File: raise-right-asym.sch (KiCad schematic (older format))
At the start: 83 parts, among them IC1 ATTINY88-A, P1 CONN_01X04, P2 CONN_01X04, P4 CONN_01X04, P6 CONN_02X03, SW1 SW_PUSH, SW10 SW_PUSH, SW11 SW_PUSH, SW12 SW_PUSH, SW13 SW_PUSH, SW14 SW_PUSH, SW15 SW_PUSH, SW16 SW_PUSH, SW17 SW_PUSH, SW18 SW_PUSH, SW19 SW_PUSH, SW2 SW_PUSH, SW20 SW_PUSH, SW21 SW_PUSH, SW22 SW_PUSH, SW23 SW_PUSH, SW24 SW_PUSH, SW25 SW_PUSH, SW26 SW_PUSH, SW27 SW_PUSH, SW28 SW_PUSH, SW29 SW_PUSH, SW3 SW_PUSH, SW30 SW_PUSH, SW31 SW_PUSH, SW32 SW_PUSH, SW33 SW_PUSH, SW34 SW_PUSH, SW4 SW_PUSH, SW5 SW_PUSH, SW6 SW_PUSH, SW7 SW_PUSH, SW8 SW_PUSH, SW9 SW_PUSH

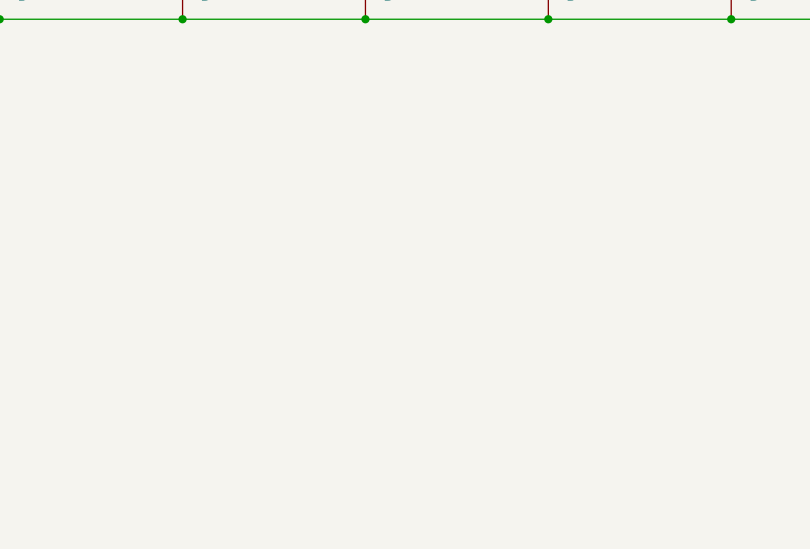
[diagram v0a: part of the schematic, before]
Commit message: note on number of keys
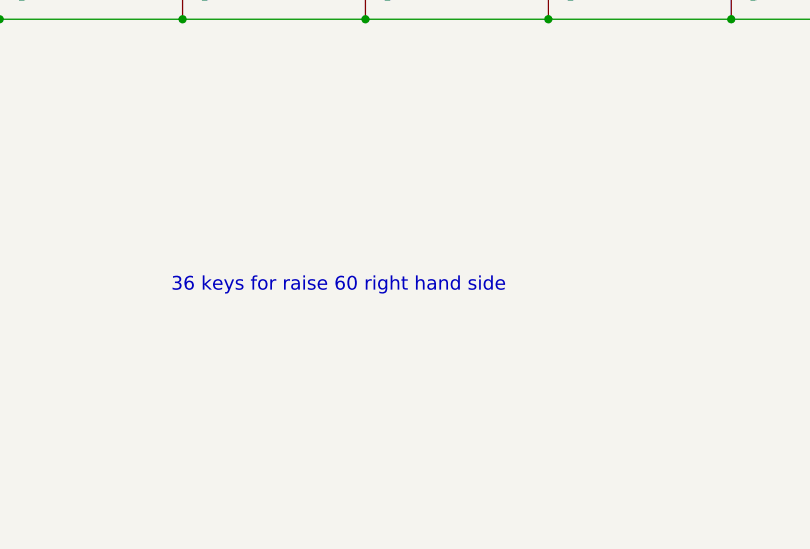
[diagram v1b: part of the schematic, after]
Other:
- note added: "36 keys for raise 60 right hand side"
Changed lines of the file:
@@
 Connection ~ 10850 3750
 Connection ~ 10850 5600
+Text Notes 7600 6800 0    60   ~ 0
+36 keys for raise 60 right hand side
 $EndSCHEMATC

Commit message: key layout for v4
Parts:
- removed D30, D35, D36: D, Diodes_SMD:SOD-123, symbol D
- removed P1, P2, P4: CONN_01X04, Pin_Headers:Pin_Header_Straight_1x04, symbol CONN_01X04
- removed P6: CONN_02X03, Pin_Headers:Pin_Header_Straight_2x03, symbol CONN_02X03
- removed led1, led2, led3: ws2812b, fp:WS2812B, symbol ws2812b
- added C3, C4: 0.1u, Capacitors_SMD:C_0805, symbol C
- added C5: 10u, Capacitors_SMD:C_0805, symbol C
- added C8: CP, Capacitors_Tantalum_SMD:TantalC_SizeC_EIA-6032_Reflow, symbol CP
- added D31: D, Diodes_SMD:SOD-123, symbol D
- added P1: CONN_02X03, Pin_Headers:Pin_Header_Straight_2x03, symbol CONN_02X03
- added P10, P7, P8, P9: CONN_01X01, fp:mount-hole-3mm, symbol CONN_01X01
- added P2: CONN_01X05, Pin_Headers:Pin_Header_Straight_1x05, symbol CONN_01X05
- added P4: USB_OTG, fp:USB MICRO B - top, symbol USB_OTG
- added P5: CONN_01X04, Pin_Headers:Pin_Header_Straight_1x04, symbol CONN_01X04
- added P6: CONN_01X04, fp:FPC_4, symbol CONN_01X04
- added Q1: Q_PMOS_GDS, TO_SOT_Packages_SMD:SOT-223, symbol Q_PMOS_GDS
- added R1: 100k, Resistors_SMD:R_0805, symbol R
- added R3, R4, R5, R7: 10k, Resistors_SMD:R_0805, symbol R
- added R6: 4.7k, Resistors_SMD:R_0805, symbol R
- added U1: TCA4311A, Housings_SSOP:MSOP-8_3x3mm_Pitch0.65mm, symbol TCA4311A
- added W1: TEST_1P, Measurement_Points:Measurement_Point_Square-TH_Small, symbol TEST_1P
- C1: value C -> 0.1u; footprint Capacitors_SMD:C_1206 -> Capacitors_SMD:C_0805
- C2: value C -> 1u; footprint Capacitors_SMD:C_1206 -> Capacitors_SMD:C_0805
- IC1: footprint Housings_QFP:TQFP-32_7x7mm_Pitch0.8mm -> Housings_QFP:LQFP-32_5x5mm_Pitch0.5mm
- R-bit0: renamed from R-add0; footprint Resistors_SMD:R_1206 -> Resistors_SMD:R_0805
- R-bit1: renamed from R-add1; footprint Resistors_SMD:R_1206 -> Resistors_SMD:R_0805
- R2: footprint Resistors_SMD:R_1206 -> Resistors_SMD:R_0805
- SW1, SW11, SW12, SW13, SW16, SW17, SW18, SW2, SW21, SW22, SW23, SW26, SW27, SW28, SW3, SW33, SW6, SW7, SW8: footprint fp:CHERRY_MX -> fp:kailhsocket-cherry
- renumbered D31 to D30
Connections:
- net labels added: +5VA, MISO, MOSI, SCK, SHUTDOWN, SLED_CS, scl_in, sda_in
- net labels removed: lp1.1, lp1.2, lp2.1, lp2.2, miso, mosi, sck, ws2812
- wire segments 33 -> 40
- no-connect marks 6 -> 7
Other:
- note added: "2 extra switches are on another PCB"
- note added: "RHS has 36 keys - 2 on breakout = 34.\n18 leds for edge, 36 for keys, 16 palms. 70 in total\n\n"
- note added: "soft start"
- note added: "top mount"
- note removed: "36 keys for raise 60 right hand side"
- note removed: "low profile breakout"
- moved on the sheet: C1, C2, D1, D10, D11, D12, D13, D14, D15, D16, D17, D18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

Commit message: led fp
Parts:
- removed P6: CONN_01X04, fp:FPC_4, symbol CONN_01X04
- added P11: CONN_01X01, Mounting_Holes:MountingHole_6mm, symbol CONN_01X01
- added P12: CONN_01X10, fp:FPC_10, symbol CONN_01X10
- added P6: CONN_01X01, fp:mount-hole-3mm, symbol CONN_01X01
- P10: footprint fp:mount-hole-3mm -> Mounting_Holes:MountingHole_6mm
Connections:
- net labels added: ca9, cb1, cb2, cb4, cb5, cb6
- wire segments 40 -> 110
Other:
- note removed: "RHS has 36 keys - 2 on breakout = 34.\n18 leds for edge, 36 for keys, 16 palms. 70 in total\n\n"
- moved on the sheet: C1, C2, D1, D10, D11, D12, D13, D14, D15, D16, D17, D18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

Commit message: routing
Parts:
- added W2: TEST_1P, Measurement_Points:Measurement_Point_Square-TH_Small, symbol TEST_1P
- IC1: footprint Housings_QFP:LQFP-32_5x5mm_Pitch0.5mm -> fp:QFN-32_EP_5x5_Pitch0.5mm
- renumbered P12 to lp1
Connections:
- wire segments 110 -> 46
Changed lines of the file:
@@
 	1150 4350 1150 4450
 Wire Wire Line
-	650  1600 900  1600
-Wire Wire Line
-	900  1600 1100 1600
-Wire Wire Line
-	1100 1600 1150 1600
+	650  1600 1150 1600
 Connection ~ 1100 1600
 Connection ~ 900  1600
@@
 F 0 "IC1" H 2100 4757 50  0000 C CNN
 F 1 "ATTINY88-A" H 2100 4666 50  0000 C CNN
-F 2 "Housings_QFP:LQFP-32_5x5mm_Pitch0.5mm" H 2100 4575 50  0001 C CIN
+F 2 "fp:QFN-32_EP_5x5_Pitch0.5mm" H 2100 4575 50  0001 C CIN
 F 3 "" H 2100 3000 50  0000 C CNN
 F 4 "1704570" H 2100 3000 60  0001 C CNN "farnell #"
@@
 Connection ~ 5400 2700
 Wire Wire Line
-	4800 1350 4800 1750
-Wire Wire Line
-	4800 1750 4800 2400
-Wire Wire Line
-	4800 2400 4800 3050
-Wire Wire Line
-	4800 3050 4800 3600
-Wire Wire Line
-	4800 3600 4800 4250
+	4800 1350 4800 4250
 Connection ~ 4800 1750
 $Comp
@@
 Connection ~ 4800 2400
 Wire Wire Line
-	4300 3350 5400 3350
-Wire Wire Line
-	5400 3350 6200 3350
-Wire Wire Line
-	6200 3350 7000 3350
-Wire Wire Line
-	7000 3350 7800 3350
-Wire Wire Line
-	7800 3350 8600 3350
-Wire Wire Line
-	8600 3350 9400 3350
-Wire Wire Line
-	9400 3350 10200 3350
+	4300 3350 10200 3350
 Text Notes 4800 900  0    118  ~ 0
 switch matrix
@@
 Connection ~ 4800 3050
 Wire Wire Line
-	4300 4550 5400 4550
-Wire Wire Line
-	5400 4550 6200 4550
-Wire Wire Line
-	6200 4550 7000 4550
-Wire Wire Line
-	7000 4550 7800 4550
-Wire Wire Line
-	7800 4550 8600 4550
-Wire Wire Line
-	8600 4550 11000 4550
-Wire Wire Line
-	4300 3900 5400 3900
-Wire Wire Line
-	5400 3900 6200 3900
-Wire Wire Line
-	6200 3900 7000 3900
-Wire Wire Line
-	7000 3900 7800 3900
-Wire Wire Line
-	7800 3900 8600 3900
-Wire Wire Line
-	8600 3900 9400 3900
-Wire Wire Line
-	4300 2700 5400 2700
-Wire Wire Line
-	5400 2700 6200 2700
-Wire Wire Line
-	6200 2700 7000 2700
-Wire Wire Line
-	7000 2700 7800 2700
-Wire Wire Line
-	7800 2700 8600 2700
-Wire Wire Line
-	8600 2700 9400 2700
-Wire Wire Line
-	9400 2700 10200 2700
-Wire Wire Line
-	10200 2700 11000 2700
-Wire Wire Line
-	4300 2050 5400 2050
-Wire Wire Line
-	5400 2050 6200 2050
-Wire Wire Line
-	6200 2050 7000 2050
-Wire Wire Line
-	7000 2050 7800 2050
-Wire Wire Line
-	7800 2050 8600 2050
-Wire Wire Line
-	8600 2050 9400 2050
-Wire Wire Line
-	9400 2050 10200 2050
+	4300 4550 11000 4550
+Wire Wire Line
+	4300 3900 9400 3900
+Wire Wire Line
+	4300 2700 11000 2700
+Wire Wire Line
+	4300 2050 10200 2050
 $Comp
 L SW_PUSH SW6
@@
 Connection ~ 6200 2700
 Wire Wire Line
-	5600 1350 5600 1750
-Wire Wire Line
-	5600 1750 5600 2400
-Wire Wire Line
-	5600 2400 5600 3050
-Wire Wire Line
-	5600 3050 5600 3600
-Wire Wire Line
-	5600 3600 5600 4250
+	5600 1350 5600 4250
 Connection ~ 5600 1750
 $Comp
@@
 Connection ~ 7000 2700
 Wire Wire Line
-	6400 1350 6400 1750
-Wire Wire Line
-	6400 1750 6400 2400
-Wire Wire Line
-	6400 2400 6400 3050
-Wire Wire Line
-	6400 3050 6400 3600
-Wire Wire Line
-	6400 3600 6400 4250
+	6400 1350 6400 4250
 Connection ~ 6400 1750
 $Comp
@@
 Connection ~ 7800 2700
 Wire Wire Line
-	7200 1350 7200 1750
-Wire Wire Line
-	7200 1750 7200 2400
-Wire Wire Line
-	7200 2400 7200 3050
-Wire Wire Line
-	7200 3050 7200 3600
-Wire Wire Line
-	7200 3600 7200 4250
+	7200 1350 7200 4250
 Connection ~ 7200 1750
 $Comp
@@
 Connection ~ 8600 2700
 Wire Wire Line
-	8000 1350 8000 1750
-Wire Wire Line
-	8000 1750 8000 2400
-Wire Wire Line
-	8000 2400 8000 3050
-Wire Wire Line
-	8000 3050 8000 3600
-Wire Wire Line
-	8000 3600 8000 4250
+	8000 1350 8000 4250
 Connection ~ 8000 1750
 $Comp
@@
 Connection ~ 9400 2700
 Wire Wire Line
-	8800 1350 8800 1750
-Wire Wire Line
-	8800 1750 8800 2400
-Wire Wire Line
-	8800 2400 8800 3050
-Wire Wire Line
-	8800 3050 8800 3600
+	8800 1350 8800 3600
 Connection ~ 8800 1750
 $Comp
@@
 Connection ~ 10200 2050
 Wire Wire Line
-	9600 1350 9600 1750
-Wire Wire Line
-	9600 1750 9600 2400
-Wire Wire Line
-	9600 2400 9600 3050
+	9600 1350 9600 3050
 Connection ~ 9600 1750
 Text Label 4300 2050 2    60   ~ 0
@@
 $EndComp
 Wire Wire Line
-	4750 5750 4850 5750
-Wire Wire Line
-	4850 5750 5250 5750
-Wire Wire Line
-	6300 5750 6600 5750
-Wire Wire Line
-	6600 5750 6700 5750
+	4750 5750 5250 5750
+Wire Wire Line
+	6300 5750 6700 5750
 $Comp
 L +5V #PWR017
@@
 $EndComp
 Wire Wire Line
-	2000 6600 2200 6600
-Wire Wire Line
-	2200 6600 2800 6600
-Wire Wire Line
-	2800 6600 2900 6600
-Wire Wire Line
-	3300 6600 3550 6600
-Wire Wire Line
-	3550 6600 4000 6600
+	2000 6600 2900 6600
+Wire Wire Line
+	3300 6600 4000 6600
 Wire Wire Line
 	3100 6900 3100 7000
@@
 Connection ~ 2800 6600
 Wire Wire Line
-	2800 6950 2800 7000
-Wire Wire Line
-	2800 7000 2800 7050
+	2800 6950 2800 7050
 Connection ~ 2800 7000
 Wire Wire Line
@@
 $EndComp
 Wire Wire Line
-	10400 1350 10400 1750
-Wire Wire Line
-	10400 1750 10400 2400
-Wire Wire Line
-	10400 2400 10400 4250
+	10400 1350 10400 4250
 Text Label 10400 1350 0    60   ~ 0
 col7
@@
 	10400 5450 9850 5450
 $Comp
-L CONN_01X10 P12
+L CONN_01X10 lp1
 U 1 1 59D8E660
 P 10600 5500
-F 0 "P12" H 10678 5541 50  0000 L CNN
+F 0 "lp1" H 10678 5541 50  0000 L CNN
 F 1 "CONN_01X10" H 10678 5450 50  0000 L CNN
 F 2 "fp:FPC_10" H 10600 5500 50  0001 C CNN
@@
 	0    1    1    0
 $EndComp
+$Comp
+L TEST_1P W2
+U 1 1 59DCB845
+P 3100 7000
+F 0 "W2" V 3054 7188 50  0000 L CNN
+F 1 "TEST_1P" V 3145 7188 50  0000 L CNN
+F 2 "Measurement_Points:Measurement_Point_Square-TH_Small" H 3300 7000 50  0001 C CNN
+F 3 "" H 3300 7000 50  0000 C CNN
+	1    3100 7000
+	0    1    1    0
+$EndComp

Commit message: exported
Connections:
- no-connect marks 7 -> 13
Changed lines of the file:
@@
 	1    0    0    -1
-$EndComp
-$Comp
-L Earth #PWR031
-U 1 1 59D3CD62
-P 2350 5050
-F 0 "#PWR031" H 2350 4800 50  0001 C CNN
-F 1 "Earth" H 2350 4900 50  0001 C CNN
-F 2 "" H 2350 5050 50  0000 C CNN
-F 3 "" H 2350 5050 50  0000 C CNN
-	1    2350 5050
-	0    1    1    0
-$EndComp
-$Comp
-L Earth #PWR032
-U 1 1 59D3CFC0
-P 2350 5200
-F 0 "#PWR032" H 2350 4950 50  0001 C CNN
-F 1 "Earth" H 2350 5050 50  0001 C CNN
-F 2 "" H 2350 5200 50  0000 C CNN
-F 3 "" H 2350 5200 50  0000 C CNN
-	1    2350 5200
-	0    1    1    0
-$EndComp
-$Comp
-L Earth #PWR033
-U 1 1 59D3D0B9
-P 2350 5350
-F 0 "#PWR033" H 2350 5100 50  0001 C CNN
-F 1 "Earth" H 2350 5200 50  0001 C CNN
-F 2 "" H 2350 5350 50  0000 C CNN
-F 3 "" H 2350 5350 50  0000 C CNN
-	1    2350 5350
-	0    1    1    0
-$EndComp
-$Comp
-L Earth #PWR034
-U 1 1 59D3D1B2
-P 2350 5500
-F 0 "#PWR034" H 2350 5250 50  0001 C CNN
-F 1 "Earth" H 2350 5350 50  0001 C CNN
-F 2 "" H 2350 5500 50  0000 C CNN
-F 3 "" H 2350 5500 50  0000 C CNN
-	1    2350 5500
-	0    1    1    0
 $EndComp
 $Sheet
@@
 $EndComp
 $Comp
-L Earth #PWR035
-U 1 1 59D8FBBD
-P 2350 5650
-F 0 "#PWR035" H 2350 5400 50  0001 C CNN
-F 1 "Earth" H 2350 5500 50  0001 C CNN
-F 2 "" H 2350 5650 50  0000 C CNN
-F 3 "" H 2350 5650 50  0000 C CNN
-	1    2350 5650
-	0    1    1    0
-$EndComp
-$Comp
-L Earth #PWR036
-U 1 1 59D8FBC3
-P 2350 5800
-F 0 "#PWR036" H 2350 5550 50  0001 C CNN
-F 1 "Earth" H 2350 5650 50  0001 C CNN
-F 2 "" H 2350 5800 50  0000 C CNN
-F 3 "" H 2350 5800 50  0000 C CNN
-	1    2350 5800
-	0    1    1    0
-$EndComp
-$Comp
 L TEST_1P W2
 U 1 1 59DCB845
@@
 	0    1    1    0
 $EndComp
+NoConn ~ 2350 5050
+NoConn ~ 2350 5200
+NoConn ~ 2350 5350
+NoConn ~ 2350 5500
+NoConn ~ 2350 5650
+NoConn ~ 2350 5800
 $EndSCHEMATC

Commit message: fab with 0.16 clearance
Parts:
- IC1: footprint fp:QFN-32_EP_5x5_Pitch0.5mm -> Housings_QFP:TQFP-32_7x7mm_Pitch0.8mm
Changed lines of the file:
@@
 F 0 "IC1" H 2100 4757 50  0000 C CNN
 F 1 "ATTINY88-A" H 2100 4666 50  0000 C CNN
-F 2 "fp:QFN-32_EP_5x5_Pitch0.5mm" H 2100 4575 50  0001 C CIN
+F 2 "Housings_QFP:TQFP-32_7x7mm_Pitch0.8mm" H 2100 4575 50  0001 C CIN
 F 3 "" H 2100 3000 50  0000 C CNN
 F 4 "1704570" H 2100 3000 60  0001 C CNN "farnell #"

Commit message: component order codes
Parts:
- C1: farnell # (none) -> 1759167
- C2: farnell # (none) -> 1759422
- C3, C4: farnell # 1414715 -> 1759167
- C5: farnell # 1759434 -> 2611940
- C8: farnell # 2611415 -> 197051RL
- D1: farnell # (none) -> 2454043
- R-bit0, R-bit1, R2, R4, R7: farnell # (none) -> 2447553
- R1: farnell # 2008404 -> 9333738
- R6: farnell # 2073929 -> 2073784
- lp1: farnell # (none) -> 1302345
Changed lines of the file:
@@
 F 2 "Capacitors_SMD:C_0805" H 938 1600 50  0001 C CNN
 F 3 "" H 900 1750 50  0000 C CNN
+F 4 "1759422" H 900 1750 60  0001 C CNN "farnell #"
 	1    900  1750
 	1    0    0    -1
@@
 F 2 "Capacitors_SMD:C_0805" H 688 1600 50  0001 C CNN
 F 3 "" H 650 1750 50  0000 C CNN
+F 4 "1759167" H 650 1750 60  0001 C CNN "farnell #"
 	1    650  1750
 	1    0    0    -1
@@
 F 2 "Resistors_SMD:R_0805" V 1630 5550 50  0001 C CNN
 F 3 "" H 1700 5550 50  0000 C CNN
+F 4 "2447553" H 1700 5550 60  0001 C CNN "farnell #"
 	1    1700 5550
 	1    0    0    -1
@@
 F 2 "Resistors_SMD:R_0805" V 1280 5550 50  0001 C CNN
 F 3 "" H 1350 5550 50  0000 C CNN
+F 4 "2447553" H 1350 5550 60  0001 C CNN "farnell #"
 	1    1350 5550
 	1    0    0    -1
@@
 F 2 "Resistors_SMD:R_0805" V 880 5550 50  0001 C CNN
 F 3 "" H 950 5550 50  0000 C CNN
+F 4 "2447553" H 950 5550 60  0001 C CNN "farnell #"
 	1    950  5550
 	1    0    0    -1
@@
 F 2 "Diodes_SMD:SOD-123" H 5400 1900 50  0001 C CNN
 F 3 "" H 5400 1900 50  0000 C CNN
+F 4 "2454043" H 5400 1900 60  0001 C CNN "farnell #"
 	1    5400 1900
 	0    -1   -1   0
@@
 F 2 "Resistors_SMD:R_0805" V 4980 5500 50  0001 C CNN
 F 3 "" H 5050 5500 50  0000 C CNN
-F 4 "2008404" H 5050 5500 60  0001 C CNN "farnell #"
+F 4 "9333738" H 5050 5500 60  0001 C CNN "farnell #"
 	1    5050 5500
 	1    0    0    -1
@@
 F 2 "Capacitors_SMD:C_0805" H 5088 6000 50  0001 C CNN
 F 3 "" H 5050 6150 50  0000 C CNN
-F 4 "1414715" H 5050 6150 60  0001 C CNN "farnell #"
+F 4 "1759167" H 5050 6150 60  0001 C CNN "farnell #"
 	1    5050 6150
 	1    0    0    -1
@@
 F 2 "Resistors_SMD:R_0805" V 6530 5600 50  0001 C CNN
 F 3 "" H 6600 5600 50  0000 C CNN
+F 4 "2447553" H 6600 5600 60  0001 C CNN "farnell #"
 	1    6600 5600
 	1    0    0    -1
@@
 F 2 "Capacitors_SMD:C_0805" H 4788 6000 50  0001 C CNN
 F 3 "" H 4750 6150 50  0000 C CNN
-F 4 "1414715" H 4750 6150 60  0001 C CNN "farnell #"
+F 4 "1759167" H 4750 6150 60  0001 C CNN "farnell #"
 	1    4750 6150
 	1    0    0    -1
@@
 F 2 "Capacitors_SMD:C_0805" H 2838 6650 50  0001 C CNN
 F 3 "" H 2800 6800 50  0000 C CNN
-F 4 "1759434" H 2800 6800 60  0001 C CNN "farnell #"
+F 4 "2611940" H 2800 6800 60  0001 C CNN "farnell #"
 	1    2800 6800
 	1    0    0    -1
@@
 F 2 "Resistors_SMD:R_0805" V 2730 7200 50  0001 C CNN
 F 3 "" H 2800 7200 50  0000 C CNN
-F 4 "2073929" H 2800 7200 60  0001 C CNN "farnell #"
+F 4 "2073784" H 2800 7200 60  0001 C CNN "farnell #"
 	1    2800 7200
 	1    0    0    -1
@@
 F 2 "Capacitors_Tantalum_SMD:TantalC_SizeC_EIA-6032_Reflow" H 4038 6700 50  0001 C CNN
 F 3 "" H 4000 6850 50  0000 C CNN
-F 4 "2611415" H 4000 6850 60  0001 C CNN "farnell #"
+F 4 "197051RL" H 4000 6850 60  0001 C CNN "farnell #"
 	1    4000 6850
 	1    0    0    -1
@@
 F 2 "Resistors_SMD:R_0805" V 3330 5350 50  0001 C CNN
 F 3 "" H 3400 5350 50  0000 C CNN
+F 4 "2447553" H 3400 5350 60  0001 C CNN "farnell #"
 	1    3400 5350
 	1    0    0    -1
@@
 F 2 "fp:FPC_10" H 10600 5500 50  0001 C CNN
 F 3 "" H 10600 5500 50  0000 C CNN
+F 4 "1302345" H 10600 5500 60  0001 C CNN "farnell #"
 	1    10600 5500
 	1    0    0    -1

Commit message: fixes for v4.2
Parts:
- P4: footprint fp:USB MICRO B - top -> fp:USB MICRO B; symbol USB_OTG -> USB_OTG-RESCUE-raise-right-asym
- SW10, SW14, SW15, SW19, SW20, SW24, SW25, SW29, SW30, SW31, SW32, SW34, SW4, SW5, SW9: footprint fp:CHERRY_MX -> fp:kailhsocket-cherry
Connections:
- net labels added: ca8
- wire segments 46 -> 47
- no-connect marks 13 -> 12
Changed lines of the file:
@@
 EESchema Schematic File Version 2
+LIBS:raise-right-asym-rescue
 LIBS:power
 LIBS:device
@@
 LIBS:rgbled
 LIBS:raise-right-asym-cache
-EELAYER 26 0
+EELAYER 25 0
 EELAYER END
 $Descr A4 11693 8268
@@
 F 0 "SW4" H 5100 3855 50  0000 C CNN
 F 1 "SW_PUSH" H 5100 3764 50  0000 C CNN
-F 2 "fp:CHERRY_MX" H 5100 3600 50  0001 C CNN
+F 2 "fp:kailhsocket-cherry" H 5100 3600 50  0001 C CNN
 F 3 "" H 5100 3600 50  0000 C CNN
 	1    5100 3600
@@
 F 0 "SW5" H 5100 4505 50  0000 C CNN
 F 1 "SW_PUSH" H 5100 4414 50  0000 C CNN
-F 2 "fp:CHERRY_MX" H 5100 4250 50  0001 C CNN
+F 2 "fp:kailhsocket-cherry" H 5100 4250 50  0001 C CNN
 F 3 "" H 5100 4250 50  0000 C CNN
 	1    5100 4250
@@
 F 0 "SW9" H 5900 3855 50  0000 C CNN
 F 1 "SW_PUSH" H 5900 3764 50  0000 C CNN
-F 2 "fp:CHERRY_MX" H 5900 3600 50  0001 C CNN
+F 2 "fp:kailhsocket-cherry" H 5900 3600 50  0001 C CNN
 F 3 "" H 5900 3600 50  0000 C CNN
 	1    5900 3600
@@
 F 0 "SW10" H 5900 4505 50  0000 C CNN
 F 1 "SW_PUSH" H 5900 4414 50  0000 C CNN
-F 2 "fp:CHERRY_MX" H 5900 4250 50  0001 C CNN
+F 2 "fp:kailhsocket-cherry" H 5900 4250 50  0001 C CNN
 F 3 "" H 5900 4250 50  0000 C CNN
 	1    5900 4250
@@
 F 0 "SW14" H 6700 3855 50  0000 C CNN
 F 1 "SW_PUSH" H 6700 3764 50  0000 C CNN
-F 2 "fp:CHERRY_MX" H 6700 3600 50  0001 C CNN
+F 2 "fp:kailhsocket-cherry" H 6700 3600 50  0001 C CNN
 F 3 "" H 6700 3600 50  0000 C CNN
 	1    6700 3600
@@
 F 0 "SW15" H 6700 4505 50  0000 C CNN
 F 1 "SW_PUSH" H 6700 4414 50  0000 C CNN
-F 2 "fp:CHERRY_MX" H 6700 4250 50  0001 C CNN
+F 2 "fp:kailhsocket-cherry" H 6700 4250 50  0001 C CNN
 F 3 "" H 6700 4250 50  0000 C CNN
 	1    6700 4250
@@
 F 0 "SW19" H 7500 3855 50  0000 C CNN
 F 1 "SW_PUSH" H 7500 3764 50  0000 C CNN
-F 2 "fp:CHERRY_MX" H 7500 3600 50  0001 C CNN
+F 2 "fp:kailhsocket-cherry" H 7500 3600 50  0001 C CNN
 F 3 "" H 7500 3600 50  0000 C CNN
 	1    7500 3600
@@
 F 0 "SW20" H 7500 4505 50  0000 C CNN
 F 1 "SW_PUSH" H 7500 4414 50  0000 C CNN
-F 2 "fp:CHERRY_MX" H 7500 4250 50  0001 C CNN
+F 2 "fp:kailhsocket-cherry" H 7500 4250 50  0001 C CNN
 F 3 "" H 7500 4250 50  0000 C CNN
 	1    7500 4250
@@
 F 0 "SW24" H 8300 3855 50  0000 C CNN
 F 1 "SW_PUSH" H 8300 3764 50  0000 C CNN
-F 2 "fp:CHERRY_MX" H 8300 3600 50  0001 C CNN
+F 2 "fp:kailhsocket-cherry" H 8300 3600 50  0001 C CNN
 F 3 "" H 8300 3600 50  0000 C CNN
 	1    8300 3600
@@
 F 0 "SW25" H 8300 4505 50  0000 C CNN
 F 1 "SW_PUSH" H 8300 4414 50  0000 C CNN
-F 2 "fp:CHERRY_MX" H 8300 4250 50  0001 C CNN
+F 2 "fp:kailhsocket-cherry" H 8300 4250 50  0001 C CNN
 F 3 "" H 8300 4250 50  0000 C CNN
 	1    8300 4250
@@
 F 0 "SW29" H 9100 3855 50  0000 C CNN
 F 1 "SW_PUSH" H 9100 3764 50  0000 C CNN
-F 2 "fp:CHERRY_MX" H 9100 3600 50  0001 C CNN
+F 2 "fp:kailhsocket-cherry" H 9100 3600 50  0001 C CNN
 F 3 "" H 9100 3600 50  0000 C CNN
 	1    9100 3600
@@
 F 0 "SW30" H 9900 2005 50  0000 C CNN
 F 1 "SW_PUSH" H 9900 1914 50  0000 C CNN
-F 2 "fp:CHERRY_MX" H 9900 1750 50  0001 C CNN
+F 2 "fp:kailhsocket-cherry" H 9900 1750 50  0001 C CNN
 F 3 "" H 9900 1750 50  0000 C CNN
 	1    9900 1750
@@
 $EndComp
 $Comp
-L USB_OTG P4
+L USB_OTG-RESCUE-raise-right-asym P4
 U 1 1 59D16A8E
 P 5300 6950
 F 0 "P4" V 5423 7138 50  0000 L CNN
 F 1 "USB_OTG" V 5332 7138 50  0000 L CNN
-F 2 "fp:USB MICRO B - top" V 5250 6850 50  0001 C CNN
+F 2 "fp:USB MICRO B" V 5250 6850 50  0001 C CNN
 F 3 "http://www.molex.com/pdm_docs/sd/1051640001_sd.pdf" V 4650 6850 50  0000 C CNN
 F 4 "2614947" H 5300 6950 60  0001 C CNN "farnell #"
@@
 NoConn ~ 3050 1800
 NoConn ~ 3050 1900
-Text Label 10400 5650 2    60   ~ 0
+Text Label 10400 5750 2    60   ~ 0
 col5
-Text Label 10400 5750 2    60   ~ 0
+Text Label 10400 5850 2    60   ~ 0
 col6
-Text Label 10400 5850 2    60   ~ 0
+Text Label 10400 5950 2    60   ~ 0
 row7
 Wire Wire Line
@@
 Text Notes 8650 4150 0    60   ~ 0
 2 extra switches are on another PCB
-NoConn ~ 10400 5950
 Text Notes 5150 7500 0    60   ~ 0
 top mount
@@
 F 0 "SW31" H 9900 2655 50  0000 C CNN
 F 1 "SW_PUSH" H 9900 2564 50  0000 C CNN
-F 2 "fp:CHERRY_MX" H 9900 2400 50  0001 C CNN
+F 2 "fp:kailhsocket-cherry" H 9900 2400 50  0001 C CNN
 F 3 "" H 9900 2400 50  0000 C CNN
 	1    9900 2400
@@
 F 0 "SW32" H 9900 3305 50  0000 C CNN
 F 1 "SW_PUSH" H 9900 3214 50  0000 C CNN
-F 2 "fp:CHERRY_MX" H 9900 3050 50  0001 C CNN
+F 2 "fp:kailhsocket-cherry" H 9900 3050 50  0001 C CNN
 F 3 "" H 9900 3050 50  0000 C CNN
 	1    9900 3050
@@
 F 0 "SW34" H 10700 4505 50  0000 C CNN
 F 1 "SW_PUSH" H 10700 4414 50  0000 C CNN
-F 2 "fp:CHERRY_MX" H 10700 4250 50  0001 C CNN
+F 2 "fp:kailhsocket-cherry" H 10700 4250 50  0001 C CNN
 F 3 "" H 10700 4250 50  0000 C CNN
 	1    10700 4250
@@
 Text GLabel 9850 5250 0    60   Input ~ 0
 cb6
-Text GLabel 9850 5350 0    60   Input ~ 0
+Text GLabel 9850 5450 0    60   Input ~ 0
 ca9
-Text GLabel 9850 5450 0    60   Input ~ 0
+Text GLabel 9850 5550 0    60   Input ~ 0
 cb1
-Text GLabel 9850 5550 0    60   Input ~ 0
+Text GLabel 9850 5650 0    60   Input ~ 0
 cb2
 Wire Wire Line
@@
 	10400 5250 9850 5250
 Wire Wire Line
-	10400 5350 9850 5350
+	10400 5450 9850 5450
+Wire Wire Line
+	10400 5650 9850 5650
 Wire Wire Line
 	10400 5550 9850 5550
-Wire Wire Line
-	10400 5450 9850 5450
 $Comp
 L CONN_01X10 lp1
@@
 NoConn ~ 2350 5650
 NoConn ~ 2350 5800
+Text GLabel 9850 5350 0    60   Input ~ 0
+ca8
+Wire Wire Line
+	9850 5350 10400 5350
 $EndSCHEMATC
